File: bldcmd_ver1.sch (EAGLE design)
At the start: 95 parts, among them IC1 STSPIN32F0, IC2 AS5047P-ATSM, IC3 ADM4852ACPZ-REEL7, J1 DF65-3P-1.7V(21), Q1 PSMN2R4-30MLD, Q2 PSMN2R4-30MLD, Q3 PSMN2R4-30MLD, Q4 PSMN2R4-30MLD, Q5 PSMN2R4-30MLD, Q6 PSMN2R4-30MLD, SW1 SKRP

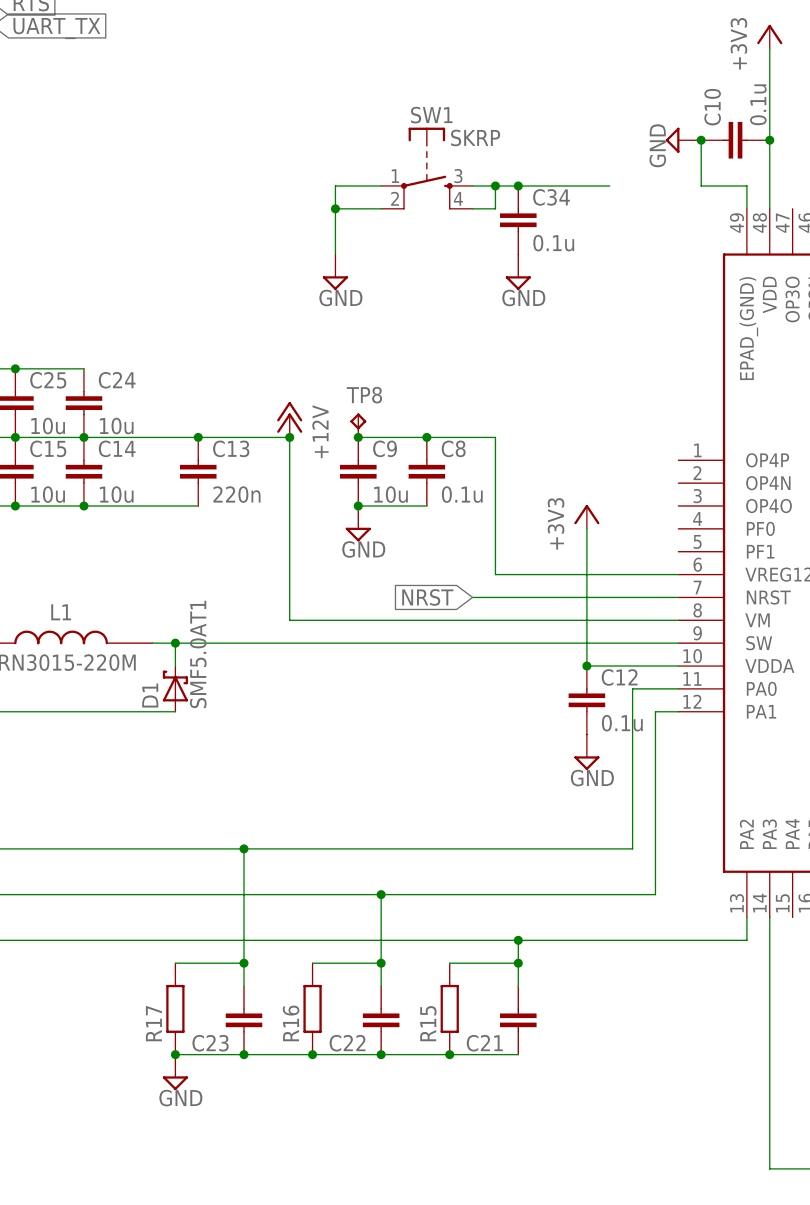
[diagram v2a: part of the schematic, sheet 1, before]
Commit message: ホールセンサのLPFのR,Cのサイズを0402から0603に変更
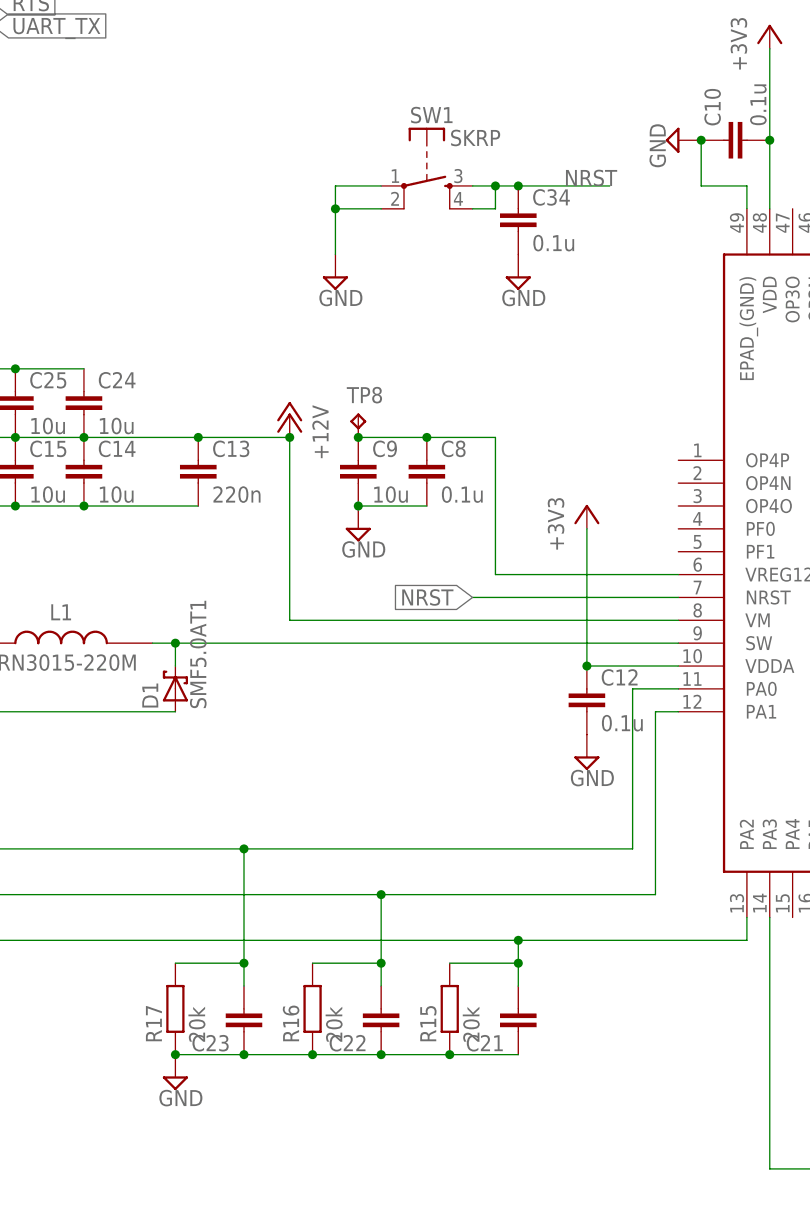
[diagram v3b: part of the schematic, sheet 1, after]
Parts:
- C21, C22, C23: device rcl:C-EUC0402 -> rcl:C-EUC0603K
- R15, R16, R17: value (none) -> 20k; device rcl:R-EU_R0402 -> rcl:R-EU_R0603
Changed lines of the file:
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@@
 <grid distance="0.1" unitdist="inch" unit="inch" style="lines" multiple="1" display="no" altdistance="0.01" altunitdist="inch" altunit="inch"/>
 <layers>
-<layer number="1" name="Top" color="4" fill="1" visible="yes" active="no"/>
-<layer number="2" name="Route2" color="1" fill="3" visible="yes" active="no"/>
-<layer number="3" name="Route3" color="4" fill="3" visible="yes" active="no"/>
-<layer number="4" name="Route4" color="1" fill="4" visible="yes" active="no"/>
-<layer number="5" name="Route5" color="4" fill="4" visible="yes" active="no"/>
-<layer number="6" name="Route6" color="1" fill="8" visible="yes" active="no"/>
-<layer number="7" name="Route7" color="4" fill="8" visible="yes" active="no"/>
-<layer number="8" name="Route8" color="1" fill="2" visible="yes" active="no"/>
-<layer number="9" name="Route9" color="4" fill="2" visible="yes" active="no"/>
-<layer number="10" name="Route10" color="1" fill="7" visible="yes" active="no"/>
-<layer number="11" name="Route11" color="4" fill="7" visible="yes" active="no"/>
-<layer number="12" name="Route12" color="1" fill="5" visible="yes" active="no"/>
-<layer number="13" name="Route13" color="4" fill="5" visible="yes" active="no"/>
-<layer number="14" name="Route14" color="1" fill="6" visible="yes" active="no"/>
-<layer number="15" name="Route15" color="4" fill="6" visible="yes" active="no"/>
-<layer number="16" name="Bottom" color="1" fill="1" visible="yes" active="no"/>
-<layer number="17" name="Pads" color="2" fill="1" visible="yes" active="no"/>
-<layer number="18" name="Vias" color="2" fill="1" visible="yes" active="no"/>
-<layer number="19" name="Unrouted" color="6" fill="1" visible="yes" active="no"/>
-<layer number="20" name="Dimension" color="24" fill="1" visible="yes" active="no"/>
-<layer number="21" name="tPlace" color="15" fill="1" visible="yes" active="no"/>
-<layer number="22" name="bPlace" color="7" fill="1" visible="yes" active="no"/>
-<layer number="23" name="tOrigins" color="15" fill="1" visible="yes" active="no"/>
-<layer number="24" name="bOrigins" color="15" fill="1" visible="yes" active="no"/>
-<layer number="25" name="tNames" color="11" fill="7" visible="yes" active="no"/>
-<layer number="26" name="bNames" color="13" fill="7" visible="yes" active="no"/>
-<layer number="27" name="tValues" color="7" fill="1" visible="yes" active="no"/>
-<layer number="28" name="bValues" color="7" fill="1" visible="yes" active="no"/>
+<layer number="1" name="Top" color="4" fill="1" visible="no" active="no"/>
+<layer number="2" name="Route2" color="1" fill="3" visible="no" active="no"/>
+<layer number="3" name="Route3" color="4" fill="3" visible="no" active="no"/>
+<layer number="4" name="Route4" color="1" fill="4" visible="no" active="no"/>
+<layer number="5" name="Route5" color="4" fill="4" visible="no" active="no"/>
+<layer number="6" name="Route6" color="1" fill="8" visible="no" active="no"/>
+<layer number="7" name="Route7" color="4" fill="8" visible="no" active="no"/>
+<layer number="8" name="Route8" color="1" fill="2" visible="no" active="no"/>
+<layer number="9" name="Route9" color="4" fill="2" visible="no" active="no"/>
+<layer number="10" name="Route10" color="1" fill="7" visible="no" active="no"/>
+<layer number="11" name="Route11" color="4" fill="7" visible="no" active="no"/>
+<layer number="12" name="Route12" color="1" fill="5" visible="no" active="no"/>
+<layer number="13" name="Route13" color="4" fill="5" visible="no" active="no"/>
+<layer number="14" name="Route14" color="1" fill="6" visible="no" active="no"/>
+<layer number="15" name="Route15" color="4" fill="6" visible="no" active="no"/>
+<layer number="16" name="Bottom" color="1" fill="1" visible="no" active="no"/>
+<layer number="17" name="Pads" color="2" fill="1" visible="no" active="no"/>
+<layer number="18" name="Vias" color="2" fill="1" visible="no" active="no"/>
+<layer number="19" name="Unrouted" color="6" fill="1" visible="no" active="no"/>
+<layer number="20" name="Dimension" color="24" fill="1" visible="no" active="no"/>
+<layer number="21" name="tPlace" color="15" fill="1" visible="no" active="no"/>
+<layer number="22" name="bPlace" color="7" fill="1" visible="no" active="no"/>
+<layer number="23" name="tOrigins" color="15" fill="1" visible="no" active="no"/>
+<layer number="24" name="bOrigins" color="15" fill="1" visible="no" active="no"/>
+<layer number="25" name="tNames" color="11" fill="7" visible="no" active="no"/>
+<layer number="26" name="bNames" color="13" fill="7" visible="no" active="no"/>
+<layer number="27" name="tValues" color="7" fill="1" visible="no" active="no"/>
+<layer number="28" name="bValues" color="7" fill="1" visible="no" active="no"/>
 <layer number="29" name="tStop" color="7" fill="3" visible="no" active="no"/>
 <layer number="30" name="bStop" color="7" fill="6" visible="no" active="no"/>
@@
 <layer number="35" name="tGlue" color="7" fill="4" visible="no" active="no"/>
 <layer number="36" name="bGlue" color="7" fill="5" visible="no" active="no"/>
-<layer number="37" name="tTest" color="7" fill="1" visible="yes" active="no"/>
-<layer number="38" name="bTest" color="7" fill="1" visible="yes" active="no"/>
+<layer number="37" name="tTest" color="7" fill="1" visible="no" active="no"/>
+<layer number="38" name="bTest" color="7" fill="1" visible="no" active="no"/>
 <layer number="39" name="tKeepout" color="4" fill="11" visible="no" active="no"/>
 <layer number="40" name="bKeepout" color="1" fill="11" visible="no" active="no"/>
@@
 <layer number="44" name="Drills" color="7" fill="1" visible="no" active="no"/>
 <layer number="45" name="Holes" color="7" fill="1" visible="no" active="no"/>
-<layer number="46" name="Milling" color="3" fill="1" visible="yes" active="no"/>
-<layer number="47" name="Measures" color="7" fill="1" visible="yes" active="no"/>
-<layer number="48" name="Document" color="7" fill="1" visible="yes" active="no"/>
-<layer number="49" name="Reference" color="7" fill="1" visible="yes" active="no"/>
-<layer number="50" name="dxf" color="7" fill="1" visible="yes" active="no"/>
-<layer number="51" name="tDocu" color="14" fill="1" visible="yes" active="no"/>
-<layer number="52" name="bDocu" color="11" fill="1" visible="yes" active="no"/>
-<layer number="53" name="tGND_GNDA" color="7" fill="1" visible="yes" active="no"/>
-<layer number="54" name="bGND_GNDA" color="7" fill="1" visible="yes" active="no"/>
-<layer number="56" name="wert" color="7" fill="1" visible="yes" active="no"/>
+<layer number="46" name="Milling" color="3" fill="1" visible="no" active="no"/>
+<layer number="47" name="Measures" color="7" fill="1" visible="no" active="no"/>
+<layer number="48" name="Document" color="7" fill="1" visible="no" active="no"/>
+<layer number="49" name="Reference" color="7" fill="1" visible="no" active="no"/>
+<layer number="50" name="dxf" color="7" fill="1" visible="no" active="no"/>
+<layer number="51" name="tDocu" color="14" fill="1" visible="no" active="no"/>
+<layer number="52" name="bDocu" color="11" fill="1" visible="no" active="no"/>
+<layer number="53" name="tGND_GNDA" color="7" fill="1" visible="no" active="no"/>
+<layer number="54" name="bGND_GNDA" color="7" fill="1" visible="no" active="no"/>
+<layer number="56" name="wert" color="7" fill="1" visible="no" active="no"/>
 <layer number="90" name="Modules" color="5" fill="1" visible="yes" active="yes"/>
 <layer number="91" name="Nets" color="2" fill="1" visible="yes" active="yes"/>
@@
 <part name="P+9" library="supply1" deviceset="+12V" device=""/>
 <part name="U$6" library="rcssl_lib" deviceset="NJM78L05A" device=""/>
-<part name="R15" library="rcl" deviceset="R-EU_" device="R0402"/>
-<part name="C21" library="rcl" deviceset="C-EU" device="C0402"/>
-<part name="C22" library="rcl" deviceset="C-EU" device="C0402"/>
-<part name="R16" library="rcl" deviceset="R-EU_" device="R0402"/>
-<part name="C23" library="rcl" deviceset="C-EU" device="C0402"/>
-<part name="R17" library="rcl" deviceset="R-EU_" device="R0402"/>
+<part name="R15" library="rcl" deviceset="R-EU_" device="R0603" value="20k"/>
+<part name="C21" library="rcl" deviceset="C-EU" device="C0603K"/>
+<part name="C22" library="rcl" deviceset="C-EU" device="C0603K"/>
+<part name="R16" library="rcl" deviceset="R-EU_" device="R0603" value="20k"/>
+<part name="C23" library="rcl" deviceset="C-EU" device="C0603K"/>
+<part name="R17" library="rcl" deviceset="R-EU_" device="R0603" value="20k"/>
 <part name="C24" library="rcl" deviceset="C-EU" device="C3216" value="10u"/>
 <part name="C25" library="rcl" deviceset="C-EU" device="C3216" value="10u"/>
@@
 <wire x1="-12.7" y1="27.94" x2="-12.7" y2="30.48" width="0.1524" layer="91"/>
 <junction x="-12.7" y="30.48"/>
-</segment>
-</net>
+<label x="-5.08" y="30.48" size="1.778" layer="95"/>
+</segment>
+</net>

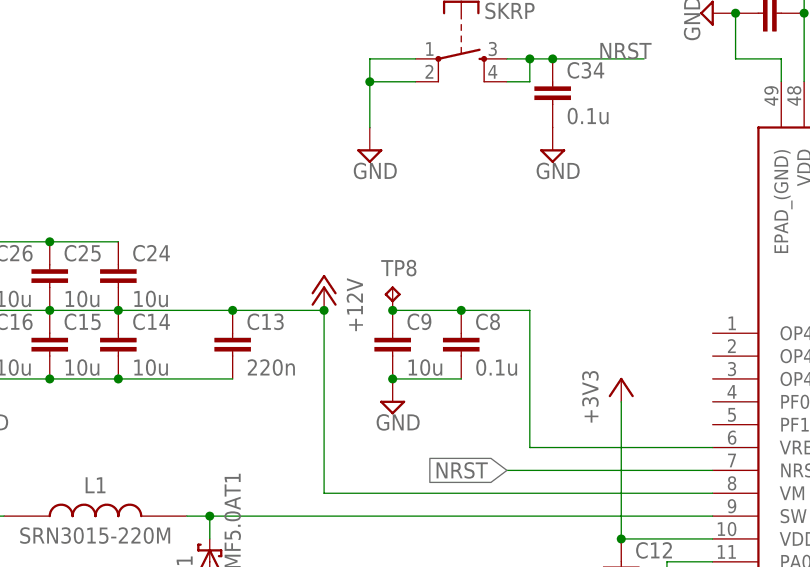
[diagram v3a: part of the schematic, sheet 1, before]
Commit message: 12Vのテストピンの削除 RSTスイッチの向きを変更
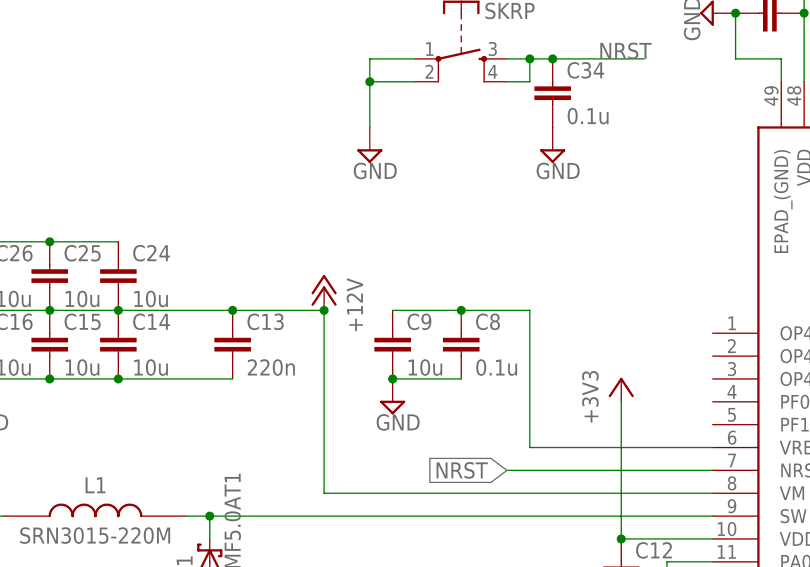
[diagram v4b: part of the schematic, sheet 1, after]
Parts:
- removed TP8: TPB1,27, testpad:TPB1,27
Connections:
- net N$19: no longer TP8.TP
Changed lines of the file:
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@@
 <part name="SUPPLY12" library="supply2" deviceset="GND" device=""/>
 <part name="+3V5" library="supply1" deviceset="+3V3" device=""/>
-<part name="TP8" library="testpad" library_urn="urn:adsk.eagle:library:385" deviceset="TP" device="B1,27" package3d_urn="urn:adsk.eagle:package:27944/1" value="TPB1,27"/>
 <part name="SUPPLY13" library="supply2" deviceset="GND" device=""/>
 <part name="R14" library="rcl" deviceset="R-EU_" device="R0402"/>
@@
 <instance part="SUPPLY12" gate="GND" x="-73.66" y="-7.62"/>
 <instance part="+3V5" gate="G$1" x="-2.54" y="-5.08"/>
-<instance part="TP8" gate="G$1" x="-27.94" y="5.08"/>
 <instance part="SUPPLY13" gate="GND" x="-2.54" y="-33.02"/>
 <instance part="R14" gate="G$1" x="78.74" y="-53.34"/>
@@
 <pinref part="C8" gate="G$1" pin="1"/>
 <junction x="-20.32" y="2.54"/>
-<pinref part="TP8" gate="G$1" pin="TP"/>
-<junction x="-27.94" y="2.54"/>
-</segment>
-</net>
+</segment>
+</net>

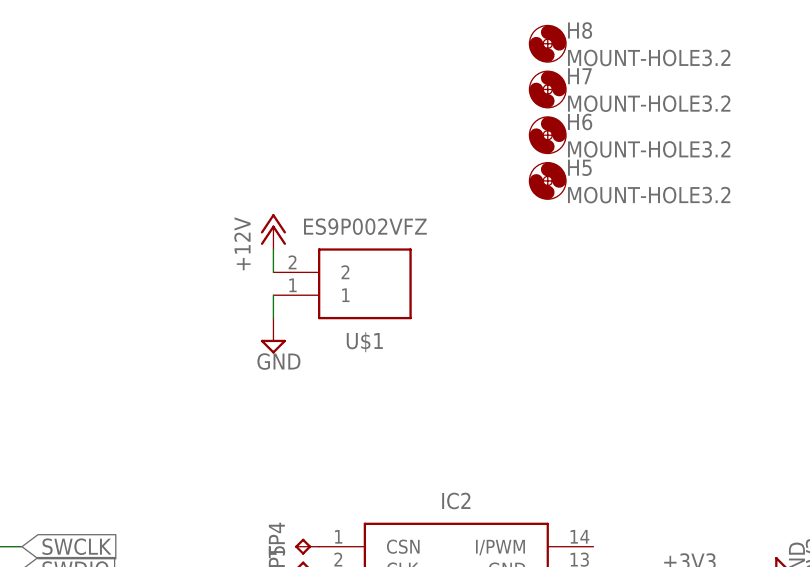
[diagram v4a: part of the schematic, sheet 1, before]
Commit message: 電源コネクタをES9からDF61に変更
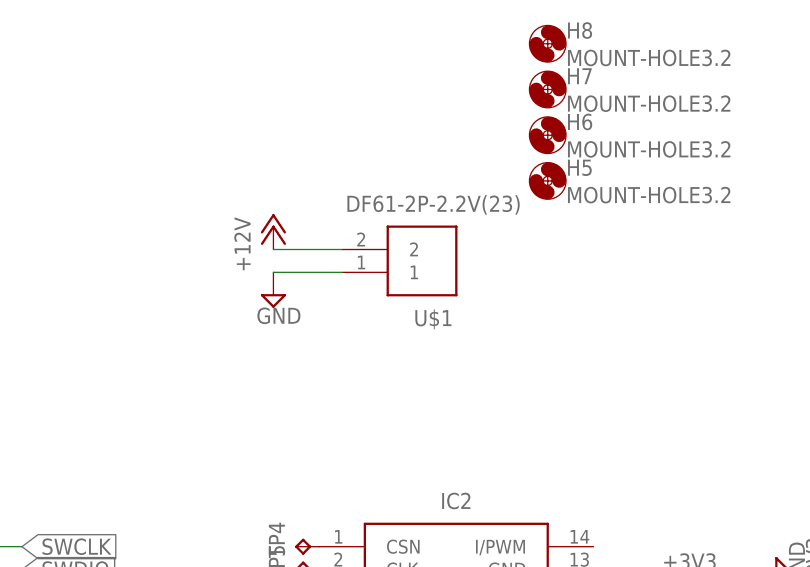
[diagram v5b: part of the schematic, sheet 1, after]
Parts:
- U$1: value ES9P002VFZ -> DF61-2P-2.2V(23); device rcssl_lib:ES9P002VFZ -> SamacSys_Parts:DF61-2P-2.2V(23)
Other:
- moved on the sheet: U$1
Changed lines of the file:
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@@
 <?xml version="1.0" encoding="utf-8"?>
 <!DOCTYPE eagle SYSTEM "eagle.dtd">
-<eagle version="8.3.2">
+<eagle version="8.4.0">
 <drawing>
 <settings>
@@
 <part name="D1" library="diode" deviceset="SMF5.0AT1" device=""/>
 <part name="C12" library="rcl" deviceset="C-EU" device="C0603K" value="0.1u"/>
-<part name="U$1" library="rcssl_lib" deviceset="ES9P002VFZ" device=""/>
+<part name="U$1" library="SamacSys_Parts" deviceset="DF61-2P-2.2V(23)" device=""/>
 <part name="SUPPLY11" library="supply2" deviceset="GND" device=""/>
 <part name="P+1" library="supply1" deviceset="+12V" device=""/>
@@
 <instance part="C12" gate="G$1" x="-2.54" y="-25.4"/>
 <instance part="U$1" gate="G$1" x="88.9" y="63.5" rot="MR180"/>
-<instance part="SUPPLY11" gate="GND" x="81.28" y="55.88"/>
+<instance part="SUPPLY11" gate="GND" x="81.28" y="60.96"/>
 <instance part="P+1" gate="1" x="81.28" y="68.58"/>
 <instance part="P+3" gate="1" x="-35.56" y="5.08" rot="MR0"/>
@@
 <segment>
 <pinref part="SUPPLY11" gate="GND" pin="GND"/>
-<wire x1="81.28" y1="60.96" x2="81.28" y2="58.42" width="0.1524" layer="91"/>
+<wire x1="88.9" y1="63.5" x2="81.28" y2="63.5" width="0.1524" layer="91"/>
 <pinref part="U$1" gate="G$1" pin="1"/>
 </segment>
@@
 <segment>
 <pinref part="P+1" gate="1" pin="+12V"/>
-<wire x1="81.28" y1="63.5" x2="81.28" y2="66.04" width="0.1524" layer="91"/>
+<wire x1="88.9" y1="66.04" x2="81.28" y2="66.04" width="0.1524" layer="91"/>
 <pinref part="U$1" gate="G$1" pin="2"/>
 </segment>

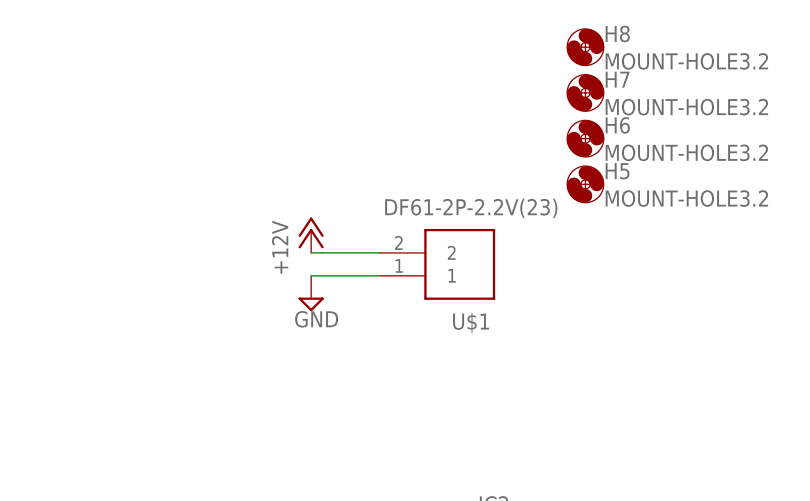
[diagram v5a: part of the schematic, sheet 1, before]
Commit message: DF61-2P-2.2V(23) の修正を適用
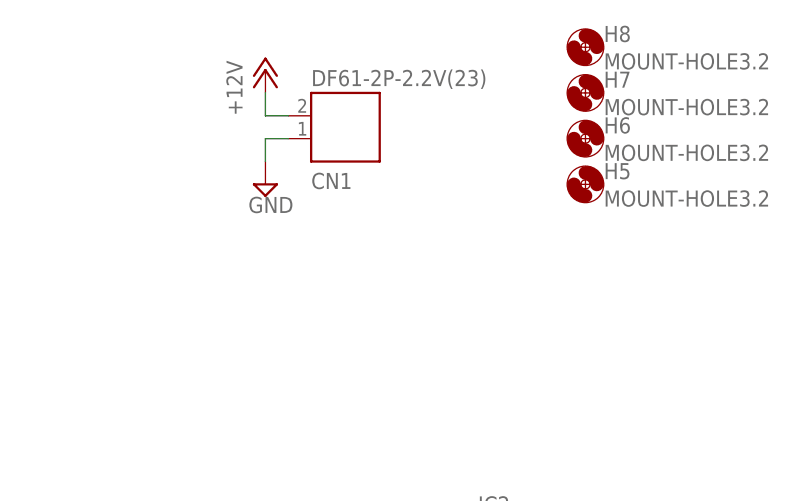
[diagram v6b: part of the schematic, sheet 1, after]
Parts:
- removed U$1: DF61-2P-2.2V(23), SamacSys_Parts:DF61-2P-2.2V(23)
- added CN1: DF61-2P-2.2V(23), SamacSys_Parts:DF61-2P-2.2V(23)
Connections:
- net +12V: now also CN1.2; no longer U$1.2
- net GND: now also CN1.1; no longer U$1.1
